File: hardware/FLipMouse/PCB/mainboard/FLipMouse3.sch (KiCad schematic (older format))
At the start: 90 parts, among them J1 SJ2-3574A, J2 SJ2-3574A, J3 M50-3900542, J4 Conn_ARM_JTAG_SWD_10, J5 Conn_02x05_Odd_Even, J6 USB_OTG, J7 Conn_01x06, Q1 BC847, Q2 BC847, Q3 BSH108, Q4 BSH108, Q5 Si2301, SW1 SW_Push, SW2 SW_Push, U1 ESP32-WROOM, U2 TSOP4838, U3 LPC11U24FBD, U4 TSR_1-2433, U5 MPXV7007GP, U6 AP2127N-3.3, Y1 JA-12.000-18-DFE

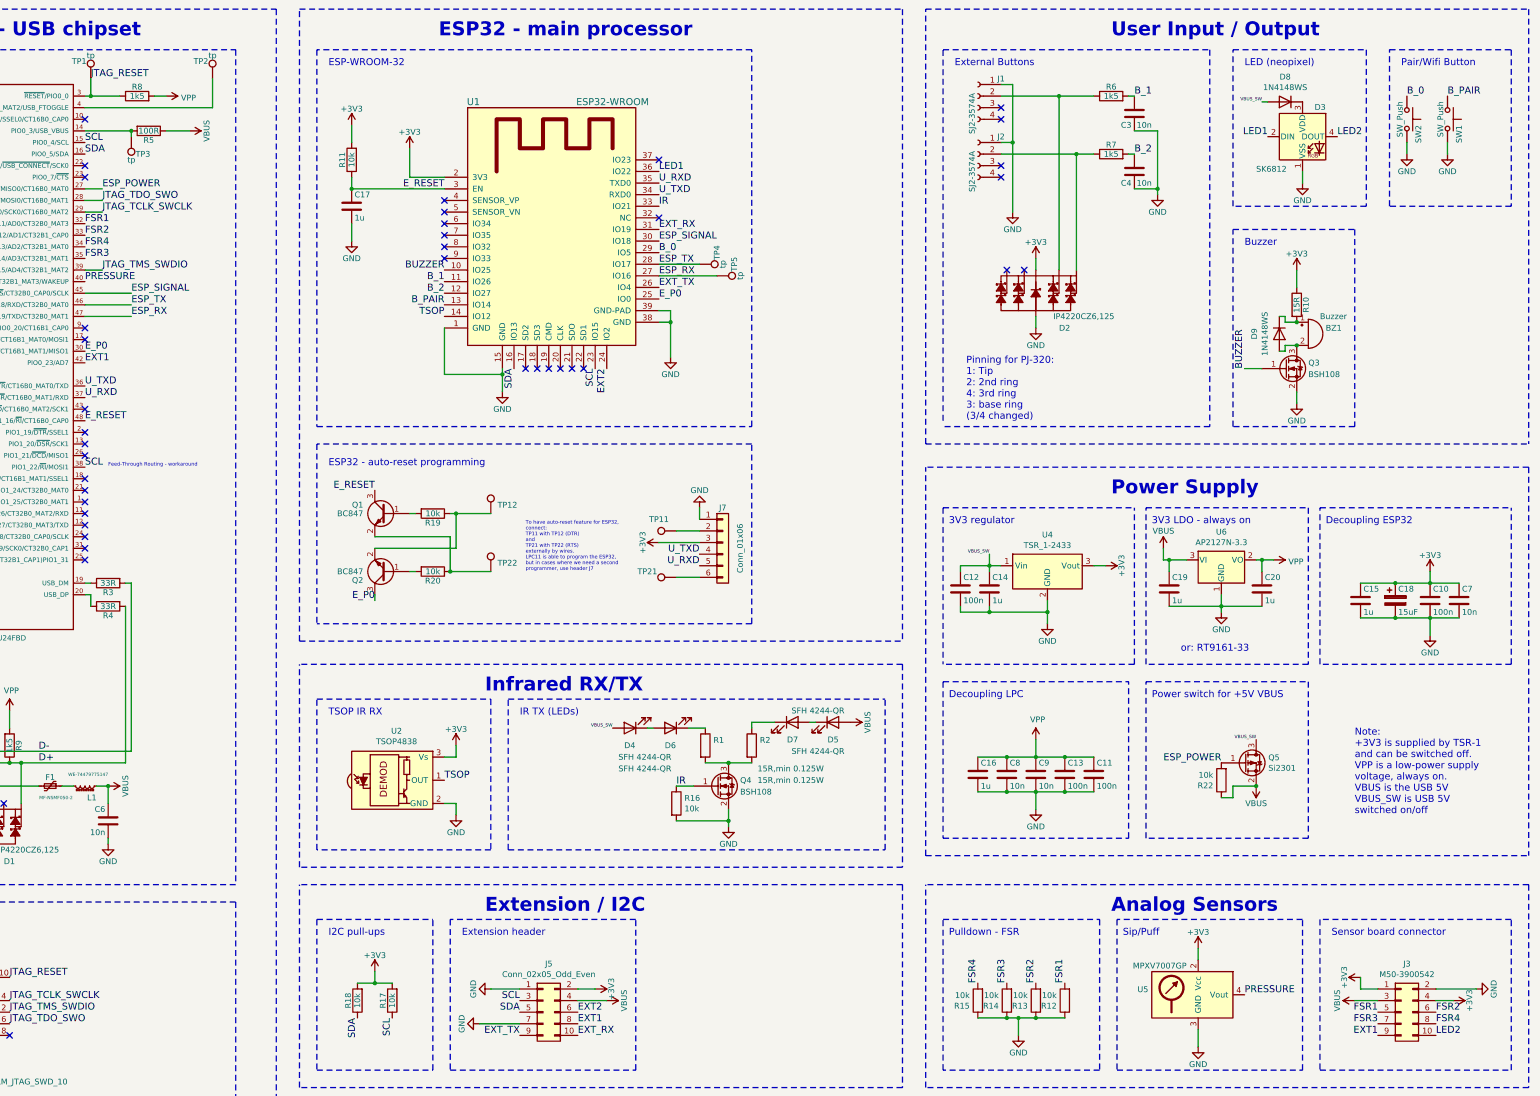
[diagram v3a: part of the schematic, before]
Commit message: First finished PCB for prototype B (no DRC errors, everything is routed & checklist is done)
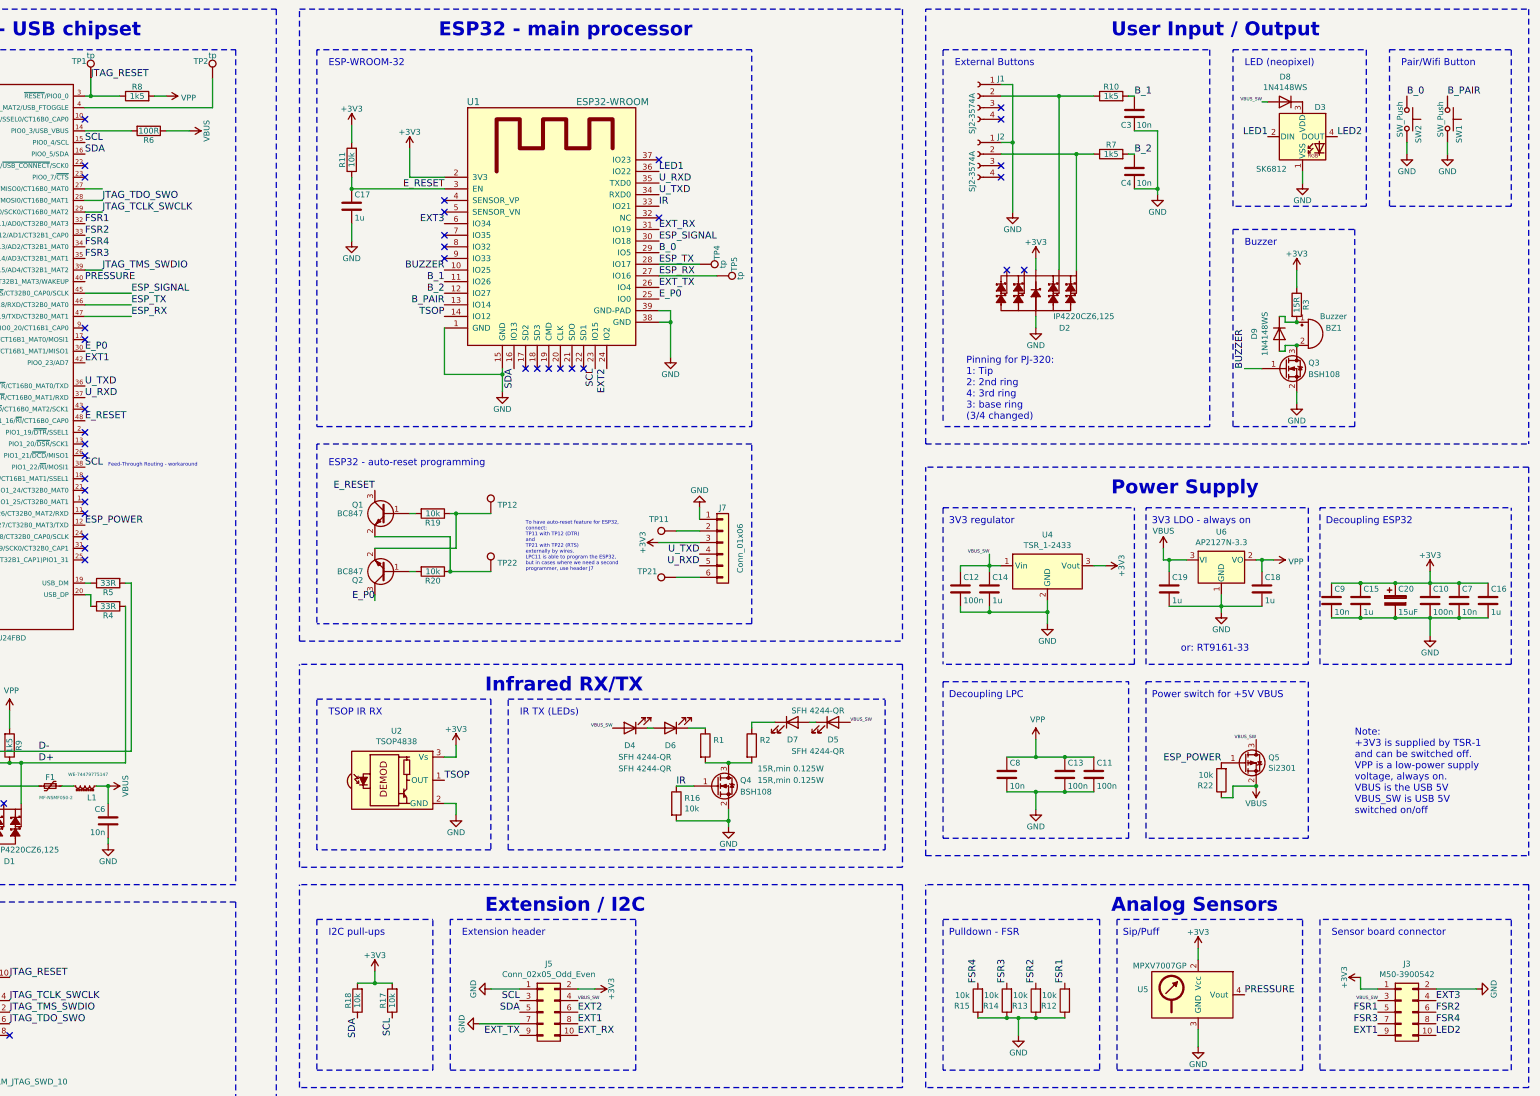
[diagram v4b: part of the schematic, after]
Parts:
- removed TP3: tp, Measurement_Points:Measurement_Point_Round-SMD-Pad_Small, symbol Connector:TestPoint
- renumbered C20 to C18, C18 to C20, R6 to R10, R10 to R3, R3 to R5, R5 to R6
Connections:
- net +3V3: now also C16.1, C9.1; no longer J3.4 (Pin_4)
- net ESP_POWER: now also U3.12 (PIO1_27/CT32B0_MAT3/TXD); no longer U3.27 (PIO0_8/MISO0/CT16B0_MAT0)
- net VBUS: no longer D5.2 (A), J3.3 (Pin_3), J5.4 (Pin_4)
- net VBUS_SW: now also D5.2 (A), J3.3 (Pin_3), J5.4 (Pin_4)
- net VPP: no longer C16.1, C9.1
- net EXT3: now reaches U1.6 (IO34)
- net EXT3: now also J3.4 (Pin_4)
- no-connect marks 40 -> 38
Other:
- moved on the sheet: C16, C9
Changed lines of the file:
@@
 Title "FLipMouse3"
 Date "2018-12-02"
-Rev "v3.1"
+Rev "v3.1b"
 Comp "AsTeRICS Foundation"
 Comment1 ""
@@
 $EndComp
 $Comp
-L Device:R R6
+L Device:R R10
 U 1 1 5A81B94F
 P 12350 1300
-F 0 "R6" V 12430 1300 50  0000 C CNN
+F 0 "R10" V 12430 1300 50  0000 C CNN
 F 1 "1k5" V 12350 1300 50  0000 C CNN
 F 2 "Resistor_SMD:R_0603_1608Metric" V 12280 1300 50  0001 C CNN
@@
 $EndComp
 $Comp
-L Device:R R10
+L Device:R R3
 U 1 1 5A81C7FF
 P 13950 3100
-F 0 "R10" V 14030 3100 50  0000 C CNN
+F 0 "R3" V 14030 3100 50  0000 C CNN
 F 1 "15R" V 13950 3100 50  0000 C CNN
 F 2 "Resistor_SMD:R_0603_1608Metric" V 13880 3100 50  0001 C CNN
@@
 L Device:C C9
 U 1 1 5A81D645
-P 11700 7150
-F 0 "C9" H 11725 7250 50  0000 L CNN
-F 1 "10n" H 11725 7050 50  0000 L CNN
-F 2 "Capacitor_SMD:C_0603_1608Metric" H 11738 7000 50  0001 C CNN
-F 3 "" H 11700 7150 50  0001 C CNN
-	1    11700 7150
+P 14250 5650
+F 0 "C9" H 14275 5750 50  0000 L CNN
+F 1 "10n" H 14275 5550 50  0000 L CNN
+F 2 "Capacitor_SMD:C_0603_1608Metric" H 14288 5500 50  0001 C CNN
+F 3 "" H 14250 5650 50  0001 C CNN
+	1    14250 5650
 	1    0    0    -1
 $EndComp
@@
 $EndComp
 $Comp
-L Device:R R3
+L Device:R R5
 U 1 1 5A81D7FE
 P 3700 5500
-F 0 "R3" V 3780 5500 50  0000 C CNN
+F 0 "R5" V 3780 5500 50  0000 C CNN
 F 1 "33R" V 3700 5500 50  0000 C CNN
 F 2 "Resistor_SMD:R_0603_1608Metric" V 3630 5500 50  0001 C CNN
@@
 $EndComp
 $Comp
-L Device:R R5
+L Device:R R6
 U 1 1 5A81DB41
 P 4050 1600
-F 0 "R5" V 4130 1600 50  0000 C CNN
+F 0 "R6" V 4130 1600 50  0000 C CNN
 F 1 "100R" V 4050 1600 50  0000 C CNN
 F 2 "Resistor_SMD:R_0603_1608Metric" V 3980 1600 50  0001 C CNN
@@
 Text Label 3900 3000 0    60   ~ 0
 ESP_SIGNAL
-Text Label 3650 2100 0    60   ~ 0
+Text Label 3500 5000 0    60   ~ 0
 ESP_POWER
 $Comp
@@
 LED1
 $Comp
-L Device:CP C18
+L Device:CP C20
 U 1 1 5A81B5B8
 P 14800 5650
-F 0 "C18" H 14825 5750 50  0000 L CNN
+F 0 "C20" H 14825 5750 50  0000 L CNN
 F 1 "15uF" H 14825 5550 50  0000 L CNN
 F 2 "Capacitor_Tantalum_SMD:CP_EIA-3216-18_Kemet-A" H 14838 5500 50  0001 C CNN
@@
 	1    0    0    -1
 $EndComp
-NoConn ~ 3500 5000
 NoConn ~ 3500 4900
 Text Label 7200 3650 3    60   ~ 0
@@
 	1    3550 1150
 	1    0    0    -1
-$EndComp
-$Comp
-L Connector:TestPoint TP3
-U 1 1 5AC522D8
-P 3900 1650
-F 0 "TP3" H 3800 1800 50  0000 C CNN
-F 1 "tp" H 3900 1850 50  0000 C CNN
-F 2 "Measurement_Points:Measurement_Point_Round-SMD-Pad_Small" H 4100 1650 50  0001 C CNN
-F 3 "" H 4100 1650 50  0001 C CNN
-	1    3900 1650
-	-1   0    0    1
 $EndComp
 $Comp
@@
 Wire Wire Line
 	11700 7000 11700 6850
-Wire Wire Line
-	11200 7000 11450 7000
 Connection ~ 1300 1600
 Wire Wire Line
@@
 Connection ~ 11950 7000
 Connection ~ 11700 7000
-Connection ~ 11450 7000
-Connection ~ 11450 7300
 Connection ~ 11700 7300
 Connection ~ 11950 7300
-Wire Wire Line
-	11200 7300 11450 7300
 Wire Wire Line
 	11700 7450 11700 7300
@@
 L Device:C C16
 U 1 1 5AC62802
-P 11200 7150
-F 0 "C16" H 11225 7250 50  0000 L CNN
-F 1 "1u" H 11225 7050 50  0000 L CNN
-F 2 "Capacitor_SMD:C_0805_2012Metric" H 11238 7000 50  0001 C CNN
-F 3 "" H 11200 7150 50  0001 C CNN
-	1    11200 7150
+P 15600 5650
+F 0 "C16" H 15625 5750 50  0000 L CNN
+F 1 "1u" H 15625 5550 50  0000 L CNN
+F 2 "Capacitor_SMD:C_0805_2012Metric" H 15638 5500 50  0001 C CNN
+F 3 "" H 15600 5650 50  0001 C CNN
+	1    15600 5650
 	1    0    0    -1
 $EndComp
@@
 	6700 4900 7000 4900
 Wire Wire Line
-	15100 5500 15350 5500
-Wire Wire Line
 	15100 5800 15350 5800
 Wire Wire Line
@@
 	-1   0    0    1
 $EndComp
-$Comp
-L power:VBUS #PWR0106
-U 1 1 5BC0718B
-P 14450 9100
-F 0 "#PWR0106" H 14450 8950 50  0001 C CNN
-F 1 "VBUS" H 14450 9250 50  0000 C CNN
-F 2 "" H 14450 9100 50  0001 C CNN
-F 3 "" H 14450 9100 50  0001 C CNN
-	1    14450 9100
-	0    -1   1    0
-$EndComp
 Text Label 14300 1650 0    60   ~ 0
 LED2
@@
 	9750 6700 9800 6700
 $Comp
-L power:VBUS #PWR0109
-U 1 1 5BBDDBED
-P 10100 6700
-F 0 "#PWR0109" H 10100 6550 50  0001 C CNN
-F 1 "VBUS" H 10100 6850 50  0000 C CNN
-F 2 "" H 10100 6700 50  0001 C CNN
-F 3 "" H 10100 6700 50  0001 C CNN
-	1    10100 6700
-	0    1    1    0
-$EndComp
-$Comp
 L power:+3V3 #PWR0110
 U 1 1 5BBFD4DB
@@
 $EndComp
 $Comp
-L power:VBUS #PWR0112
-U 1 1 5BC1F4E0
-P 8000 9100
-F 0 "#PWR0112" H 8000 8950 50  0001 C CNN
-F 1 "VBUS" H 8000 9250 50  0000 C CNN
-F 2 "" H 8000 9100 50  0001 C CNN
-F 3 "" H 8000 9100 50  0001 C CNN
-	1    8000 9100
-	0    1    -1   0
-$EndComp
-$Comp
 L power:GND #PWR0114
 U 1 1 5BC2A529
@@
 Wire Wire Line
 	11550 9400 11550 9250
-Wire Wire Line
-	14450 9100 14650 9100
 Text Label 14650 9200 2    60   ~ 0
 FSR1
@@
 Wire Wire Line
 	7900 9000 7750 9000
-Wire Wire Line
-	8000 9100 7750 9100
 Text Label 7250 9200 2    60   ~ 0
 SDA
@@
 Wire Wire Line
 	3500 1400 4600 1400
-Wire Wire Line
-	3900 1650 3900 1600
-Connection ~ 3900 1600
 Wire Wire Line
 	3500 1600 3900 1600
@@
 Wire Wire Line
 	13300 5700 13650 5700
-Wire Wire Line
-	15500 9000 15150 9000
-$Comp
-L power:+3V3 #PWR042
-U 1 1 5C908208
-P 15300 9100
-F 0 "#PWR042" H 15300 8950 50  0001 C CNN
-F 1 "+3V3" H 15300 9240 50  0000 C CNN
-F 2 "" H 15300 9100 50  0001 C CNN
-F 3 "" H 15300 9100 50  0001 C CNN
-	1    15300 9100
-	0    1    1    0
-$EndComp
-Wire Wire Line
-	15300 9100 15150 9100
 Text Label 13650 1350 2    28   ~ 0
 VBUS_SW
@@
 NoConn ~ 6600 2200
 NoConn ~ 6600 2300
-NoConn ~ 6600 2400
 NoConn ~ 6600 2500
 NoConn ~ 6600 2600
@@
 $EndComp
 $Comp
-L Device:C C20
+L Device:C C18
 U 1 1 5C8BF936
 P 13650 5550
-F 0 "C20" H 13675 5650 50  0000 L CNN
+F 0 "C18" H 13675 5650 50  0000 L CNN
 F 1 "1u" H 13675 5450 50  0000 L CNN
 F 2 "Capacitor_SMD:C_0805_2012Metric" H 13688 5400 50  0001 C CNN
@@
 	13100 8650 13100 8750
 NoConn ~ 3500 2000
+Text Label 14650 9100 2    28   ~ 0
+VBUS_SW
+Text Label 6600 2400 2    60   ~ 0
+EXT3
+Text Label 15150 9100 0    60   ~ 0
+EXT3
+Wire Wire Line
+	15150 9000 15500 9000
+Text Label 7750 9100 0    28   ~ 0
+VBUS_SW
+Text Label 10100 6700 0    28   ~ 0
+VBUS_SW
+Wire Wire Line
+	15100 5500 15350 5500
+Connection ~ 15350 5500
+Wire Wire Line
+	15350 5500 15600 5500
+Wire Wire Line
+	15600 5800 15350 5800
+Connection ~ 15350 5800
+Wire Wire Line
+	14250 5800 14500 5800
+Connection ~ 14500 5800
+Wire Wire Line
+	14250 5500 14500 5500
+Connection ~ 14500 5500
 $EndSCHEMATC

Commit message: Updated PCB, final changes & refinements for v3.1b
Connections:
- no-connect marks 38 -> 39
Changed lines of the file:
@@
 Wire Wire Line
 	8800 2750 8450 2750
-Wire Wire Line
-	3650 2100 3500 2100
 NoConn ~ 3500 4700
 Wire Wire Line
@@
 	14250 5500 14500 5500
 Connection ~ 14500 5500
+NoConn ~ 3500 2100
 $EndSCHEMATC
